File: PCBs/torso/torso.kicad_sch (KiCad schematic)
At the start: 5 parts

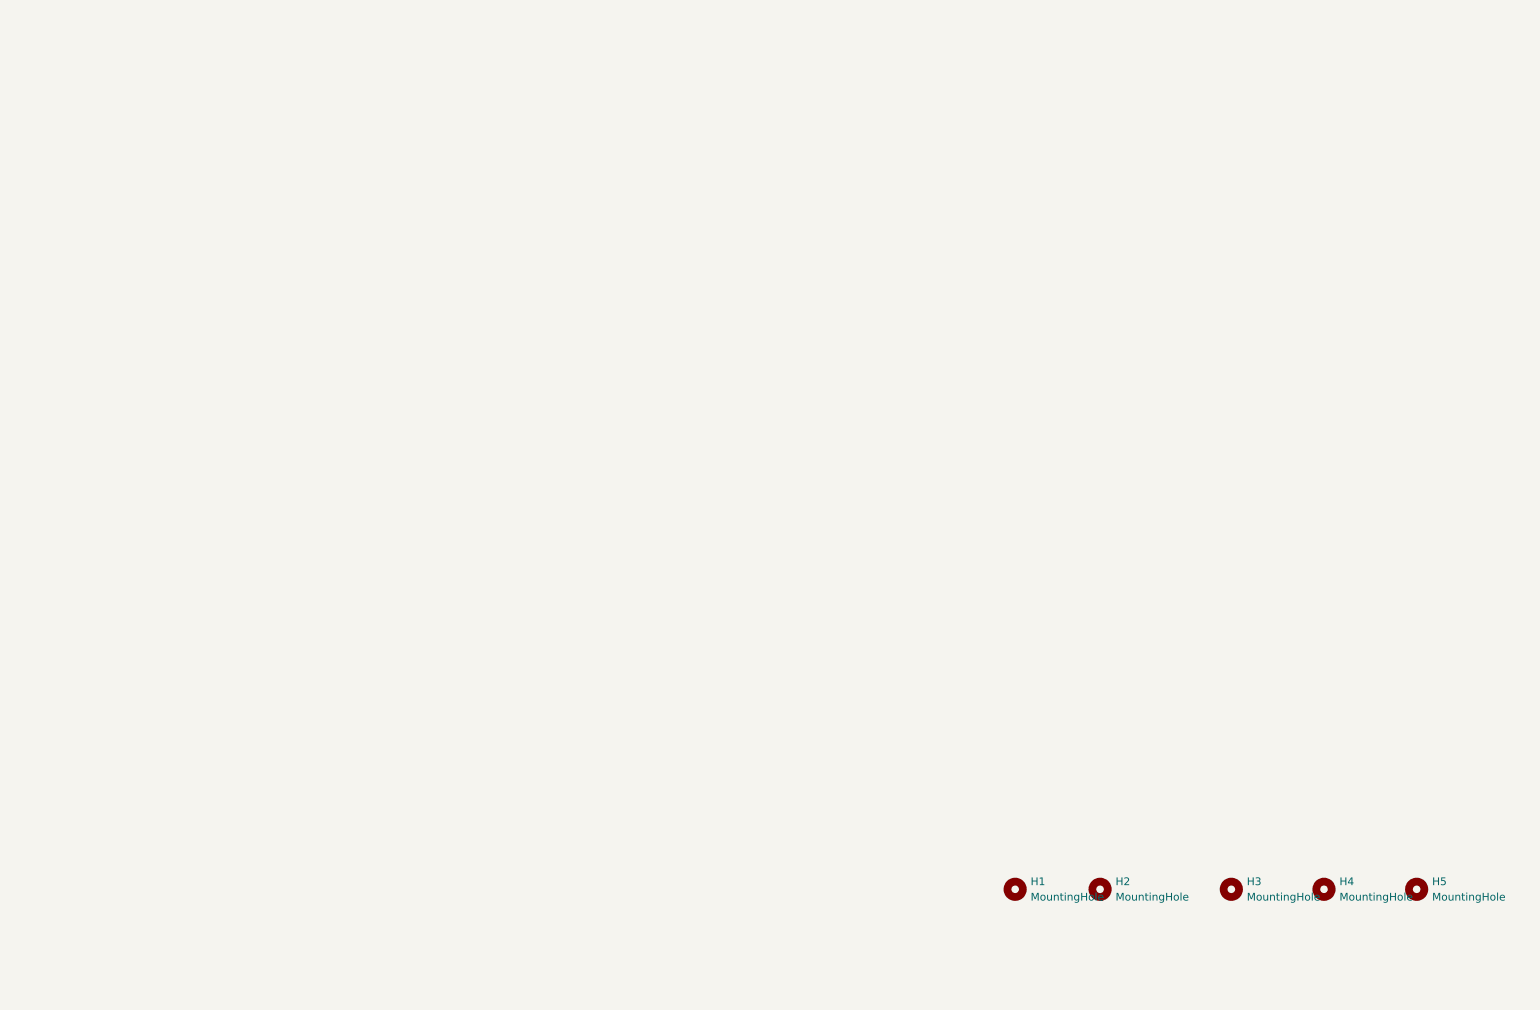
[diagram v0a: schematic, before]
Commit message: Torso all but complete, making bogie before checking the last mark
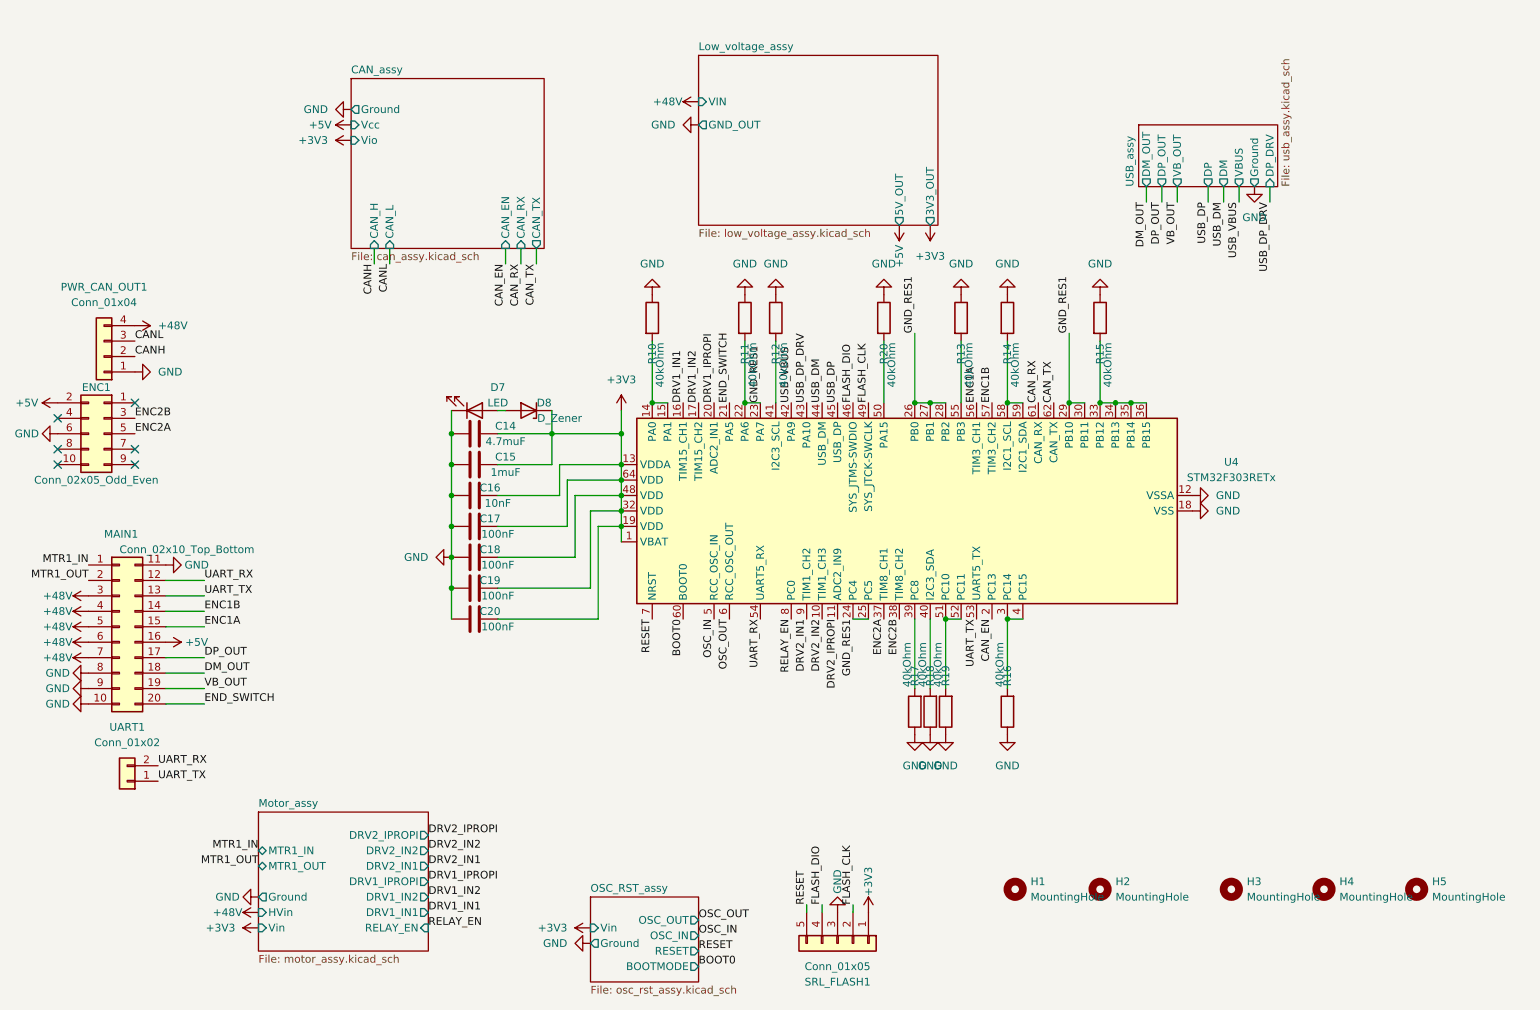
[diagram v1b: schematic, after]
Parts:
- added C14: 4.7muF, Capacitor_SMD:C_0603_1608Metric, symbol Device:C
- added C15: 1muF, Capacitor_SMD:C_0603_1608Metric, symbol Device:C
- added C16: 10nF, Capacitor_SMD:C_0603_1608Metric, symbol Device:C
- added C17, C18, C19, C20: 100nF, Capacitor_SMD:C_0603_1608Metric, symbol Device:C
- added D7: LED, LED_SMD:LED_0603_1608Metric, symbol Device:LED
- added D8: D_Zener, Diode_THT:D_T-1_P5.08mm_Horizontal, symbol Device:D_Zener
- added ENC1: Conn_02x05_Odd_Even, Connector_PinHeader_2.54mm:PinHeader_2x05_P2.54mm_Vertical, symbol Connector_Generic:Conn_02x05_Odd_Even
- added MAIN1: Conn_02x10_Top_Bottom, 1761681-7:1761681-7_TYC, symbol Connector_Generic:Conn_02x10_Top_Bottom
- added PWR_CAN_OUT1: Conn_01x04, TerminalBlock_4Ucon:TerminalBlock_4Ucon_1x04_P3.50mm_Vertical, symbol Connector_Generic:Conn_01x04
- added R10, R11, R12, R13, R14, R15, R16, R17, R18, R19, R20: 40kOhm, Resistor_SMD:R_0402_1005Metric, symbol Device:R
- added SRL_FLASH1: Conn_01x05, Connector_PinHeader_2.54mm:PinHeader_1x05_P2.54mm_Vertical, symbol Connector_Generic:Conn_01x05
- added U4: STM32F303RETx, Package_QFP:LQFP-64_10x10mm_P0.5mm, symbol MCU_ST_STM32F3:STM32F303RETx
- added UART1: Conn_01x02, Connector_PinHeader_2.54mm:PinHeader_1x02_P2.54mm_Vertical, symbol Connector_Generic:Conn_01x02
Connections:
- new net: D7.2 (A), D8.2 (A)
- new net: R17.2, U4.39 (PC8)
- new net: R16.2, U4.3 (PC14), U4.4 (PC15)
- new net: R12.2, U4.41 (PA8)
- new net: R20.2, U4.50 (PA15)
- new net: R18.2, U4.40 (PC9)
- new net: R10.2, U4.14 (PA0), U4.15 (PA1)
- new net: R15.2, U4.33 (PB12), U4.34 (PB13), U4.35 (PB14), U4.36 (PB15)
- new net: R19.2, U4.51 (PC10), U4.52 (PC11)
- new net: R13.2, U4.55 (PB3)
- new net: R14.2, U4.58 (PB6), U4.59 (PB7)
- new net +3V3: C14.1, C15.1, C16.2, C17.2, C18.2, C19.2, C20.2, D8.1 (K), SRL_FLASH1.1 (Pin_1), U4.1 (VBAT), U4.13 (VDDA), U4.19 (VDD), U4.32 (VDD), U4.48 (VDD), U4.64 (VDD)
- new net +48V: MAIN1.3 (Pin_3), MAIN1.4 (Pin_4), MAIN1.5 (Pin_5), MAIN1.6 (Pin_6), MAIN1.7 (Pin_7), PWR_CAN_OUT1.4 (48V)
- new net +5V: ENC1.2 (Pin_2), MAIN1.16 (Pin_16)
- new net BOOT0: U4.60 (BOOT0)
- new net CANH: PWR_CAN_OUT1.2 (CANH)
- new net CANL: PWR_CAN_OUT1.3 (CANL)
- new net CAN_EN: U4.2 (PC13)
- new net CAN_RX: U4.61 (PB8)
- new net CAN_TX: U4.62 (PB9)
- new net DM_OUT: MAIN1.18 (Pin_18)
- new net DP_OUT: MAIN1.17 (Pin_17)
- new net DRV1_IN1: U4.16 (PA2)
- new net DRV1_IN2: U4.17 (PA3)
- new net DRV1_IPROPI: U4.20 (PA4)
- new net DRV2_IN1: U4.9 (PC1)
- new net DRV2_IN2: U4.10 (PC2)
- new net DRV2_IPROPI: U4.11 (PC3)
- new net ENC1A: MAIN1.15 (Pin_15), U4.56 (PB4)
- new net ENC1B: MAIN1.14 (Pin_14), U4.57 (PB5)
- new net ENC2A: ENC1.5 (Pin_5), U4.37 (PC6)
- new net ENC2B: ENC1.3 (Pin_3), U4.38 (PC7)
- new net END_SWITCH: MAIN1.20 (Pin_20), U4.21 (PA5)
- new net FLASH_CLK: SRL_FLASH1.2 (Pin_2), U4.49 (PA14)
- new net FLASH_DIO: SRL_FLASH1.4 (Pin_4), U4.46 (PA13)
- new net GND: C14.2, C15.2, C16.1, C17.1, C18.1, C19.1, C20.1, D7.1 (K), ENC1.6 (Pin_6), MAIN1.10 (Pin_10), MAIN1.11 (Pin_11), MAIN1.8 (Pin_8), MAIN1.9 (Pin_9), PWR_CAN_OUT1.1 (GND), R10.1, R11.1, R12.1, R13.1, R14.1, R15.1, R16.1, R17.1, R18.1, R19.1, R20.1, SRL_FLASH1.3 (Pin_3), U4.12 (VSSA), U4.18 (VSS), U4.31 (VSS), U4.47 (VSS), U4.63 (VSS)
- new net GND_RES1: R11.2, U4.22 (PA6), U4.23 (PA7), U4.24 (PC4), U4.25 (PC5), U4.26 (PB0), U4.27 (PB1), U4.28 (PB2), U4.29 (PB10), U4.30 (PB11)
- new net MTR1_IN: MAIN1.1 (Pin_1)
- new net MTR1_OUT: MAIN1.2 (Pin_2)
- new net OSC_IN: U4.5 (PF0)
- new net OSC_OUT: U4.6 (PF1)
- new net RELAY_EN: U4.8 (PC0)
- new net RESET: SRL_FLASH1.5 (Pin_5), U4.7 (NRST)
- new net UART_RX: MAIN1.12 (Pin_12), U4.54 (PD2), UART1.2 (Pin_2)
- new net UART_TX: MAIN1.13 (Pin_13), U4.53 (PC12), UART1.1 (Pin_1)
- new net USB_DM: U4.44 (PA11)
- new net USB_DP: U4.45 (PA12)
- new net USB_DP_DRV: U4.43 (PA10)
- new net USB_VBUS: U4.42 (PA9)
- new net VB_OUT: MAIN1.19 (Pin_19)
- no-connect marks 0 -> 6
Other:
- added sheet CAN_assy (can_assy.kicad_sch)
- added sheet Low_voltage_assy (low_voltage_assy.kicad_sch)
- added sheet Motor_assy (motor_assy.kicad_sch)
- added sheet OSC_RST_assy (osc_rst_assy.kicad_sch)
- added sheet USB_assy (usb_assy.kicad_sch)

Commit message: merged changes from timertests, mostly documentation and such. Did not add tim6 config
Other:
- title: (none) -> Torso PCB
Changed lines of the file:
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@@
 (kicad_sch (version 20230121) (generator eeschema)
   (paper "A4")
+  (title_block
+    (title "Torso PCB")
+    (rev "Mk1.2")
+  )
   (junction (at 196.85 78.74) (diameter 0) (color 0 0 0 0)
   )
